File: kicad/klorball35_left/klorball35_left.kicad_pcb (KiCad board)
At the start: 2 copper layers, 138.1 x 106.1 mm, 10 parts, among them U1 Helios

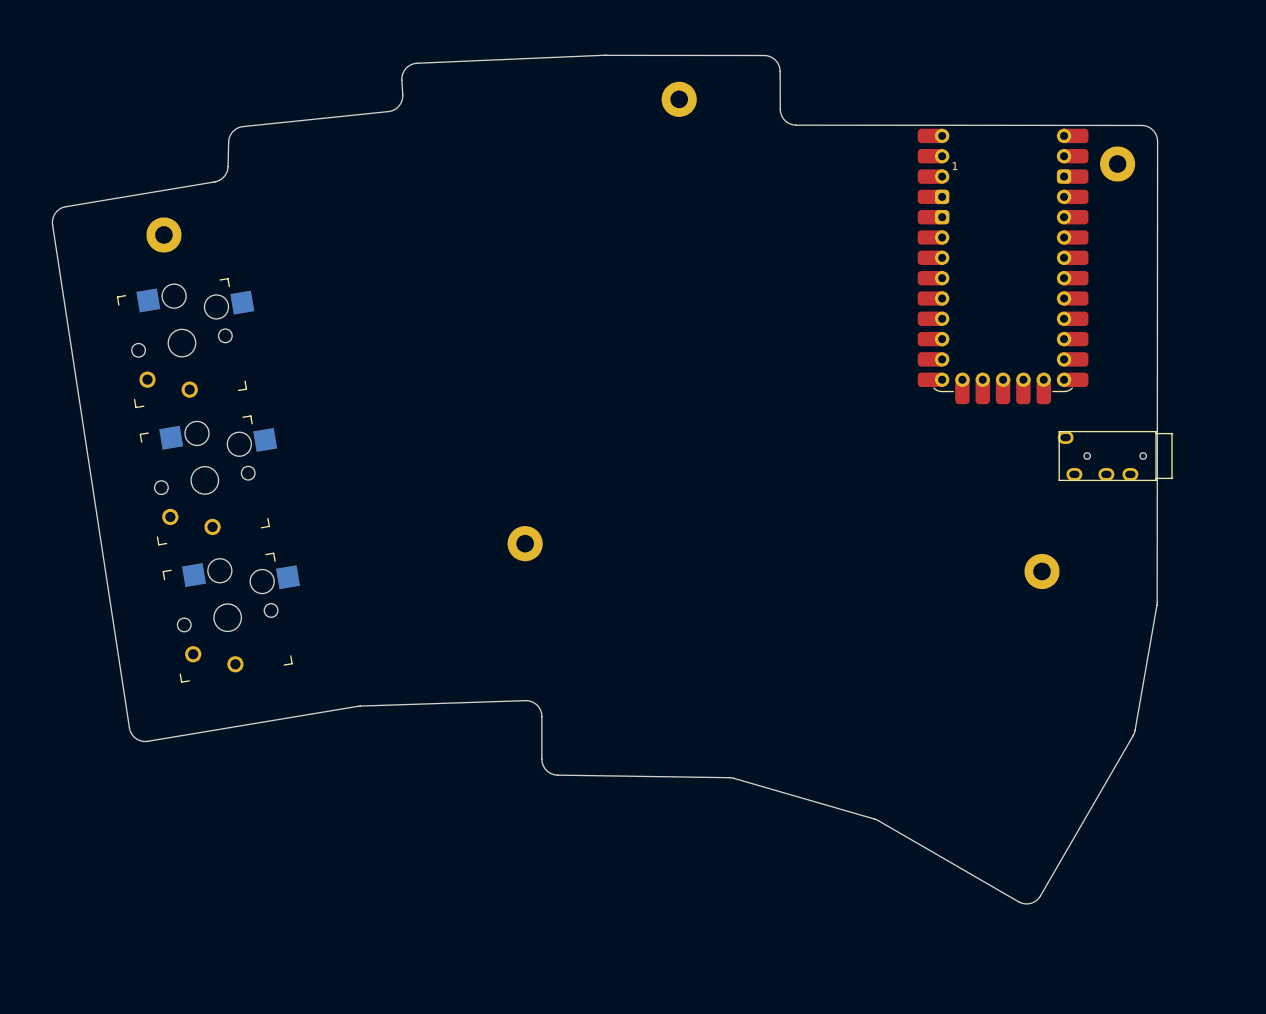
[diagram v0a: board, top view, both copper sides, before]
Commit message: Finishing footprints on left, starting schema
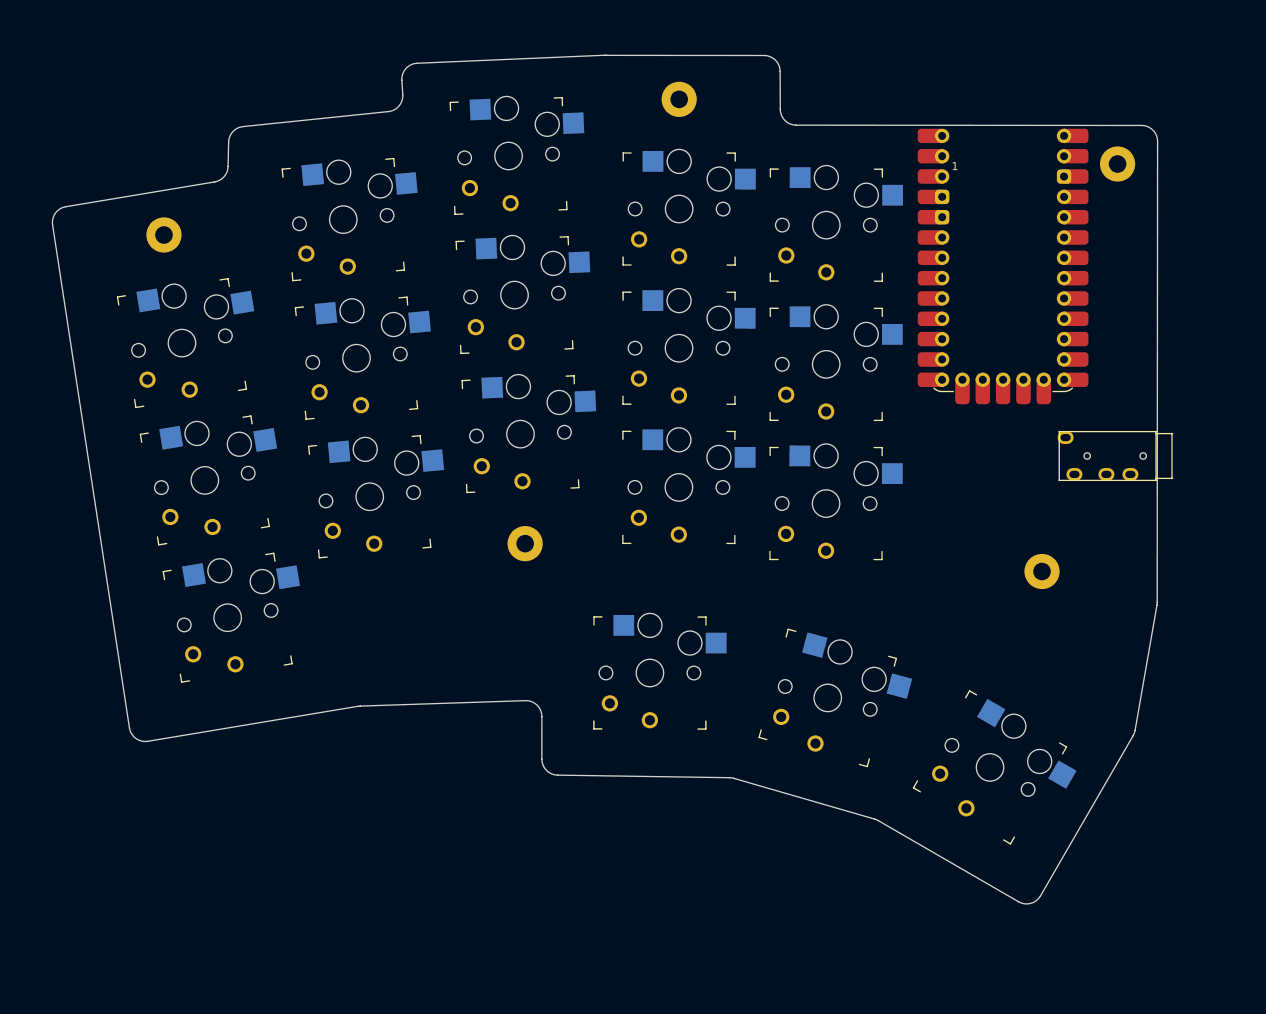
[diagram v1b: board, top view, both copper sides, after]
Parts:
- added REF**: Kailh_socket_PG1350_optional, keyswitches:Kailh_socket_PG1350_optional, F.Cu at (248.9, 100.5)
- added REF**: Kailh_socket_PG1350_optional, keyswitches:Kailh_socket_PG1350_optional, F.Cu at (230.5, 81.1)
- added REF**: Kailh_socket_PG1350_optional, keyswitches:Kailh_socket_PG1350_optional, F.Cu at (248.9, 117.9)
- added REF**: Kailh_socket_PG1350_optional, keyswitches:Kailh_socket_PG1350_optional, F.Cu at (248.9, 83.1)
- added REF**: Kailh_socket_PG1350_optional, keyswitches:Kailh_socket_PG1350_optional, F.Cu at (190.2, 99.8)
- added REF**: Kailh_socket_PG1350_optional, keyswitches:Kailh_socket_PG1350_optional, F.Cu at (230.5, 98.5)
- added REF**: Kailh_socket_PG1350_optional, keyswitches:Kailh_socket_PG1350_optional, F.Cu at (230.5, 115.9)
- added REF**: Kailh_socket_PG1350_optional, keyswitches:Kailh_socket_PG1350_optional, F.Cu at (209.2, 74.5)
- added REF**: Kailh_socket_PG1350_optional, keyswitches:Kailh_socket_PG1350_optional, F.Cu at (210.7, 109.3)
- added REF**: Kailh_socket_PG1350_optional, keyswitches:Kailh_socket_PG1350_optional, F.Cu at (226.9, 139.1)
- added REF**: Kailh_socket_PG1350_optional, keyswitches:Kailh_socket_PG1350_optional, F.Cu at (188.5, 82.5)
- added REF**: Kailh_socket_PG1350_optional, keyswitches:Kailh_socket_PG1350_optional, F.Cu at (209.9, 91.9)
- added REF**: Kailh_socket_PG1350_optional, keyswitches:Kailh_socket_PG1350_optional, F.Cu at (249.1, 142.2)
- added REF**: Kailh_socket_PG1350_optional, keyswitches:Kailh_socket_PG1350_optional, F.Cu at (269.4, 150.9)
- added REF**: Kailh_socket_PG1350_optional, keyswitches:Kailh_socket_PG1350_optional, F.Cu at (191.8, 117.1)

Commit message: Finishing left, start of right
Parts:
- J1: renamed from REF**; value TRRS-PJ-320A -> TRRS
- SW1, SW10, SW11, SW12, SW13, SW14, SW15, SW16, SW17, SW18, SW2, SW3, SW4, SW5, SW6, SW7, SW8, SW9: renamed from REF**; value Kailh_socket_PG1350_optional -> SW_Push
- moved U1 0.10 mm to (271.0, 88.6)
- renumbered H7 to H1, H7 to H2, H7 to H3, H7 to H4, H7 to H5
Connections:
- J1 pad R1: (no net) -> /TRRS_RX
- J1 pad R2: (no net) -> /TRRS_TX
- J1 pad S: (no net) -> +3V3
- J1 pad T: (no net) -> GND
- SW1 pad 1: (no net) -> /PINKY_TOP
- SW1 pad 2: (no net) -> GND
- SW10 pad 1: (no net) -> /MIDDLE_THUMB
- SW10 pad 2: (no net) -> GND
- SW11 pad 1: (no net) -> /INDEX_TOP
- SW11 pad 2: (no net) -> GND
- SW12 pad 1: (no net) -> /INDEX_HOME
- SW12 pad 2: (no net) -> GND
- SW13 pad 1: (no net) -> /INDEX_BOTTOM
- SW13 pad 2: (no net) -> GND
- SW14 pad 1: (no net) -> /INDEX_THUMB
- SW14 pad 2: (no net) -> GND
- SW15 pad 1: (no net) -> /INNER_TOP
- SW15 pad 2: (no net) -> GND
- SW16 pad 1: (no net) -> /INNER_HOME
- SW16 pad 2: (no net) -> GND
- SW17 pad 1: (no net) -> /INNER_BOTTOM
- SW17 pad 2: (no net) -> GND
- SW18 pad 1: (no net) -> /INNER_THUMB
- SW18 pad 2: (no net) -> GND
- SW2 pad 1: (no net) -> /PINKY_HOME
- SW2 pad 2: (no net) -> GND
- SW3 pad 1: (no net) -> /PINKY_BOTTOM
- SW3 pad 2: (no net) -> GND
- SW4 pad 1: (no net) -> /RING_TOP
- SW4 pad 2: (no net) -> GND
- SW5 pad 1: (no net) -> /RING_HOME
- SW5 pad 2: (no net) -> GND
- SW6 pad 1: (no net) -> /RING_BOTTOM
- SW6 pad 2: (no net) -> GND
- SW7 pad 1: (no net) -> /MIDDLE_TOP
- SW7 pad 2: (no net) -> GND
- SW8 pad 1: (no net) -> /MIDDLE_HOME
- SW8 pad 2: (no net) -> GND
- SW9 pad 1: (no net) -> /MIDDLE_BOTTOM
- SW9 pad 2: (no net) -> GND
- U1 pad 1: (no net) -> /TRRS_TX
- U1 pad 10: (no net) -> /INNER_HOME
- U1 pad 11: (no net) -> /INDEX_HOME
- U1 pad 12: (no net) -> /MIDDLE_HOME
- U1 pad 13: (no net) -> unconnected-(U1-5V-Pad13)
- U1 pad 14: (no net) -> GND
- U1 pad 15: (no net) -> unconnected-(U1-RST-Pad15)
- U1 pad 16: (no net) -> +3V3
- U1 pad 17: (no net) -> unconnected-(U1-P29-Pad17)_1
- U1 pad 18: (no net) -> unconnected-(U1-P28-Pad18)_1
- U1 pad 19: (no net) -> unconnected-(U1-P27-Pad19)_1
- U1 pad 2: (no net) -> /TRRS_RX
- U1 pad 20: (no net) -> /INNER_THUMB
- U1 pad 21: (no net) -> /INDEX_THUMB
- U1 pad 22: (no net) -> /MIDDLE_THUMB
- U1 pad 23: (no net) -> /PINKY_BOTTOM
- U1 pad 24: (no net) -> /RING_BOTTOM
- U1 pad 25: (no net) -> /RING_HOME
- U1 pad 26: (no net) -> /PINKY_HOME
- U1 pad 27: (no net) -> /INNER_BOTTOM
- U1 pad 28: (no net) -> /INDEX_BOTTOM
- U1 pad 29: (no net) -> /MIDDLE_BOTTOM
- U1 pad 3: (no net) -> GND
- U1 pad 30: (no net) -> unconnected-(U1-P11-Pad30)_1
- U1 pad 31: (no net) -> unconnected-(U1-P10-Pad31)_1
- U1 pad 4: (no net) -> GND
- U1 pad 5: (no net) -> /PINKY_TOP
- U1 pad 6: (no net) -> /RING_TOP
- U1 pad 7: (no net) -> /MIDDLE_TOP
- U1 pad 8: (no net) -> /INDEX_TOP
- U1 pad 9: (no net) -> /INNER_TOP
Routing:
- net /PINKY_BOTTOM: track 0.00 -> 147.1 mm
- net /PINKY_TOP: track 0.00 -> 126.9 mm
- net /PINKY_HOME: track 0.00 -> 124.5 mm
- net /RING_BOTTOM: track 0.00 -> 116.0 mm
- net /INDEX_THUMB: track 0.00 -> 103.3 mm
- net /RING_TOP: track 0.00 -> 98.3 mm
- net /RING_HOME: track 0.00 -> 96.0 mm
- net /MIDDLE_THUMB: track 0.00 -> 93.0 mm
- net /MIDDLE_BOTTOM: track 0.00 -> 91.8 mm
- net /INNER_THUMB: track 0.00 -> 90.2 mm
- net /MIDDLE_TOP: track 0.00 -> 74.5 mm
- net /MIDDLE_HOME: track 0.00 -> 71.3 mm
- net /INDEX_BOTTOM: track 0.00 -> 68.7 mm
- net /TRRS_TX: track 0.00 -> 60.4 mm
- net /TRRS_RX: track 0.00 -> 57.7 mm
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- added copper zone on B.Cu, net GND
- added copper zone on F.Cu, net GND

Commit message: finishing right, start of gerbers
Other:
- rule pad_to_mask_clearance: 0.05 -> 0
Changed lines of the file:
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@@
 	)
 	(setup
-		(pad_to_mask_clearance 0.05)
+		(stackup
+			(layer "F.SilkS"
+				(type "Top Silk Screen")
+			)
+			(layer "F.Paste"
+				(type "Top Solder Paste")
+			)
+			(layer "F.Mask"
+				(type "Top Solder Mask")
+				(thickness 0.01)
+			)
+			(layer "F.Cu"
+				(type "copper")
+				(thickness 0.035)
+			)
+			(layer "dielectric 1"
+				(type "core")
+				(thickness 1.51)
+				(material "FR4")
+				(epsilon_r 4.5)
+				(loss_tangent 0.02)
+			)
+			(layer "B.Cu"
+				(type "copper")
+				(thickness 0.035)
+			)
+			(layer "B.Mask"
+				(type "Bottom Solder Mask")
+				(thickness 0.01)
+			)
+			(layer "B.Paste"
+				(type "Bottom Solder Paste")
+			)
+			(layer "B.SilkS"
+				(type "Bottom Silk Screen")
+			)
+			(copper_finish "None")
+			(dielectric_constraints no)
+		)
+		(pad_to_mask_clearance 0)
 		(allow_soldermask_bridges_in_footprints no)
 		(tenting front back)
@@
 			(outputformat 1)
 			(mirror no)
-			(drillshape 1)
+			(drillshape 0)
 			(scaleselection 1)
-			(outputdirectory "")
+			(outputdirectory "../../gerbers/")
 		)
 	)
@@
 		)
 		(pad "" np_thru_hole circle
-			(at -5.499996 0 2.45)
+			(at -5.499998 0 2.45)
 			(size 1.7018 1.7018)
 			(drill 1.7018)
@@
 		)
 		(pad "" np_thru_hole circle
-			(at 5.499996 0 2.45)
+			(at 5.499998 0 2.45)
 			(size 1.7018 1.7018)
 			(drill 1.7018)
@@
 		)
 		(fp_line
+			(start -2.8 0)
+			(end -2.8 -2)
+			(stroke
+				(width 0.15)
+				(type solid)
+			)
+			(layer "F.SilkS")
+		)
+		(fp_line
+			(start 2.8 0)
+			(end 2.8 -2)
+			(stroke
+				(width 0.15)
+				(type solid)
+			)
+			(layer "F.SilkS")
+		)
+		(fp_line
 			(start 3.05 0)
 			(end 3.05 12.1)
@@
 			(layer "F.SilkS")
 		)
+		(fp_line
+			(start 2.8 -2)
+			(end -2.8 -2)
+			(stroke
+				(width 0.15)
+				(type solid)
+			)
+			(layer "F.SilkS")
+		)
 		(fp_text user "Tip"
 			(at 0 10 90)
@@
 		)
 		(pad "" np_thru_hole circle
-			(at -5.499996 0 2.45)
+			(at -5.499998 0 2.45)
 			(size 1.7018 1.7018)
 			(drill 1.7018)
@@
 		)
 		(pad "" np_thru_hole circle
-			(at 5.499996 0 2.45)
+			(at 5.499998 0 2.45)
 			(size 1.7018 1.7018)
 			(drill 1.7018)
@@
 		)
 		(pad "" np_thru_hole circle
-			(at -5.499996 0 2.45)
+			(at -5.499998 0 2.45)
 			(size 1.7018 1.7018)
 			(drill 1.7018)
@@
 		)
 		(pad "" np_thru_hole circle
-			(at 5.499996 0 2.45)
+			(at 5.499998 0 2.45)
 			(size 1.7018 1.7018)
 			(drill 1.7018)

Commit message: Wrapping up, re-organizing.  Final gerbers and designs
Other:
- board text added: "KLORBALL35 Rev. 1.0"
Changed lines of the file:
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@@
 		(sheetname "/")
 		(sheetfile "klorball35_left.kicad_sch")
-		(attr through_hole)
+		(attr through_hole exclude_from_pos_files exclude_from_bom)
 		(fp_line
 			(start -7 7)
@@
 		(sheetname "/")
 		(sheetfile "klorball35_left.kicad_sch")
-		(attr through_hole)
+		(attr through_hole exclude_from_pos_files exclude_from_bom)
 		(fp_line
 			(start -7 -6)
@@
 		(sheetname "/")
 		(sheetfile "klorball35_left.kicad_sch")
-		(attr through_hole)
+		(attr through_hole exclude_from_pos_files exclude_from_bom)
 		(fp_line
 			(start -7 7)
@@
 		(sheetname "/")
 		(sheetfile "klorball35_left.kicad_sch")
-		(attr through_hole)
+		(attr through_hole exclude_from_pos_files exclude_from_bom)
 		(fp_line
 			(start -7 -6)
@@
 		(sheetname "/")
 		(sheetfile "klorball35_left.kicad_sch")
-		(attr through_hole)
+		(attr through_hole exclude_from_pos_files exclude_from_bom)
 		(fp_line
 			(start -7 -6)
@@
 		)
 		(pad "" np_thru_hole circle
-			(at -5.499998 0 2.45)
+			(at -5.499996 0 2.45)
 			(size 1.7018 1.7018)
 			(drill 1.7018)
@@
 		)
 		(pad "" np_thru_hole circle
-			(at 5.499998 0 2.45)
+			(at 5.499996 0 2.45)
 			(size 1.7018 1.7018)
 			(drill 1.7018)
@@
 		(sheetname "/")
 		(sheetfile "klorball35_left.kicad_sch")
-		(attr through_hole)
+		(attr through_hole exclude_from_pos_files exclude_from_bom)
 		(fp_line
 			(start -7 7)
@@
 		(sheetname "/")
 		(sheetfile "klorball35_left.kicad_sch")
-		(attr through_hole)
+		(attr through_hole exclude_from_pos_files exclude_from_bom)
 		(fp_line
 			(start -7 7)
@@
 		(sheetname "/")
 		(sheetfile "klorball35_left.kicad_sch")
-		(attr through_hole)
+		(attr through_hole exclude_from_pos_files exclude_from_bom)
 		(fp_line
 			(start -7 -6)
@@
 		(sheetname "/")
 		(sheetfile "klorball35_left.kicad_sch")
-		(attr through_hole)
+		(attr through_hole exclude_from_pos_files exclude_from_bom)
 		(fp_line
 			(start -7 -6)
@@
 		(sheetname "/")
 		(sheetfile "klorball35_left.kicad_sch")
-		(attr through_hole)
+		(attr through_hole exclude_from_pos_files exclude_from_bom)
 		(fp_line
 			(start -7 7)
@@
 		(sheetname "/")
 		(sheetfile "klorball35_left.kicad_sch")
-		(attr through_hole)
+		(attr through_hole exclude_from_pos_files exclude_from_bom)
 		(fp_line
 			(start -7 7)
@@
 		(sheetname "/")
 		(sheetfile "klorball35_left.kicad_sch")
-		(attr through_hole)
+		(attr through_hole exclude_from_pos_files exclude_from_bom)
 		(fp_line
 			(start 3.05 12.1)
@@
 		(sheetname "/")
 		(sheetfile "klorball35_left.kicad_sch")
-		(attr through_hole)
+		(attr through_hole exclude_from_pos_files exclude_from_bom)
 		(fp_line
 			(start -7 -6)
@@
 			(pinfunction "GND")
 			(pintype "power_in")
+			(zone_connect 2)
 		)
 		(pad "15" thru_hole circle
@@
 		(sheetname "/")
 		(sheetfile "klorball35_left.kicad_sch")
-		(attr through_hole)
+		(attr through_hole exclude_from_pos_files exclude_from_bom)
 		(fp_line
 			(start -7 7)
@@
 		(sheetname "/")
 		(sheetfile "klorball35_left.kicad_sch")
-		(attr through_hole)
+		(attr through_hole exclude_from_pos_files exclude_from_bom)
 		(fp_line
 			(start -7 -6)
@@
 		(sheetname "/")
 		(sheetfile "klorball35_left.kicad_sch")
-		(attr through_hole)
+		(attr through_hole exclude_from_pos_files exclude_from_bom)
 		(fp_line
 			(start -7 7)
@@
 		(sheetname "/")
 		(sheetfile "klorball35_left.kicad_sch")
-		(attr through_hole)
+		(attr through_hole exclude_from_pos_files exclude_from_bom)
 		(fp_line
 			(start -7 7)
@@
 		(sheetname "/")
 		(sheetfile "klorball35_left.kicad_sch")
-		(attr through_hole)
+		(attr through_hole exclude_from_pos_files exclude_from_bom)
 		(fp_line
 			(start -7 -6)
@@
 		)
 		(pad "" np_thru_hole circle
-			(at -5.499998 0 2.45)
+			(at -5.499996 0 2.45)
 			(size 1.7018 1.7018)
 			(drill 1.7018)
@@
 		)
 		(pad "" np_thru_hole circle
-			(at 5.499998 0 2.45)
+			(at 5.499996 0 2.45)
 			(size 1.7018 1.7018)
 			(drill 1.7018)
@@
 		(sheetname "/")
 		(sheetfile "klorball35_left.kicad_sch")
-		(attr through_hole)
+		(attr through_hole exclude_from_pos_files exclude_from_bom)
 		(fp_line
 			(start -7 -6)
@@
 		)
 		(pad "" np_thru_hole circle
-			(at -5.499998 0 2.45)
+			(at -5.499996 0 2.45)
 			(size 1.7018 1.7018)
 			(drill 1.7018)
@@
 		)
 		(pad "" np_thru_hole circle
-			(at 5.499998 0 2.45)
+			(at 5.499996 0 2.45)
 			(size 1.7018 1.7018)
 			(drill 1.7018)
@@
 		(layer "Edge.Cuts")
 	)
+	(gr_text "KLORBALL35\nRev. 1.0\n"
+		(at 275.864042 136.436174 0)
+		(layer "F.SilkS")
+		(effects
+			(font
+				(size 1 1)
+				(thickness 0.2)
+				(bold yes)
+			)
+			(justify left bottom)
+		)
+	)
 	(segment
